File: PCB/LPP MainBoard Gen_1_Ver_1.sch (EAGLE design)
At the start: 46 parts, among them IC1 FE1.1S, J1 USB Type A, U1 MAX15070, U3 IFX007T, U4 MAX15070, U5 IFX007T, U7 Pill STM32G431, U8 Blue Pill STM32F103

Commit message: modified:   PCB/LPP MainBoard Gen_1_Ver_1.brd 	modified:   PCB/LPP MainBoard Gen_1_Ver_1.dch 	modified:   PCB/LPP MainBoard Gen_1_Ver_1.sch 	modified:   PCB/LPP_MainBoard_Gen_1_Ver_1.dip 	deleted:    PCB/LPP_MainBoard_Gen_1_Ver_1/Through.drl 	new file:   PCB/LPP_MainBoard_Gen_1_Ver_1/komtur.crv3d 	new file:   PCB/LPP_MainBoard_Gen_1_Ver_1/komtur.dxf 	new file:   PCB/LPP_MainBoard_Gen_1_Ver_1/kontur.txt
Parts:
- added R13, R14: R_0805_1206, common:R_0805_1206
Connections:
- net Сеть_10: now also R13.2
- net Сеть_6: now also R14.2
- net Сеть_7: now also R13.1, R14.1
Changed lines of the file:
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@@
 <part name="XP3" library="common" deviceset="PLS_2" device="" value="BKL  SEL"/>
 <part name="Z" library="common" deviceset="Q_1" device=""/>
+<part name="R13" library="common" deviceset="R_0805_1206" device=""/>
+<part name="R14" library="common" deviceset="R_0805_1206" device=""/>
 </parts>
 <modules/>
@@
 <text x="134.798" y="-214.63" size="1.48" layer="97" font="vector" ratio="10" rot="R0" align="bottom-left" distance="76">BKL  SEL</text>
 <text x="-81.045" y="-206.502" size="1.48" layer="97" font="vector" ratio="10" rot="R0" align="bottom-left" distance="76"></text>
+<text x="-39.135" y="-314.96" size="1.48" layer="97" font="vector" ratio="10" rot="R0" align="bottom-left" distance="76"></text>
+<text x="-39.135" y="-320.04" size="1.48" layer="97" font="vector" ratio="10" rot="R0" align="bottom-left" distance="76"></text>
 </plain>
 <moduleinsts/>
@@
 <instance part="XP3" gate="PART_1" x="140.335" y="-217.17" smashed="yes"/>
 <instance part="Z" gate="PART_1" x="-81.28" y="-208.28" smashed="yes"/>
+<instance part="R13" gate="PART_1" x="-39.37" y="-316.23" smashed="yes"/>
+<instance part="R14" gate="PART_1" x="-39.37" y="-321.31" smashed="yes"/>
 </instances>
 <busses/>
@@
 <pinref part="FPC" gate="PART_1" pin="13"/>
 <junction x="-22.86" y="-346.71"/>
-<wire layer="91" width="0.1" x1="-35.56" y1="-367.03" x2="-22.86" y2="-367.03"/>
+<wire layer="91" width="0.1" x1="-29.21" y1="-367.03" x2="-22.86" y2="-367.03"/>
+<wire layer="91" width="0.1" x1="-35.56" y1="-367.03" x2="-29.21" y2="-367.03"/>
 <pinref part="ENCKP" gate="PART_1" pin="2"/>
 <junction x="-22.86" y="-367.03"/>
+<wire layer="91" width="0.1" x1="-33.02" y1="-321.31" x2="-29.21" y2="-321.31"/>
+<wire layer="91" width="0.1" x1="-29.21" y1="-321.31" x2="-29.21" y2="-367.03"/>
+<pinref part="R14" gate="PART_1" pin="2"/>
+<junction x="-29.21" y="-367.03"/>
 </segment>
 </net>
@@
 <pinref part="NetPort12" gate="PART_1" pin="+5V"/>
 <junction x="-77.47" y="-331.47"/>
+<wire layer="91" width="0.1" x1="-46.99" y1="-321.31" x2="-46.99" y2="-331.47"/>
+<wire layer="91" width="0.1" x1="-46.99" y1="-331.47" x2="-66.04" y2="-331.47"/>
+<junction x="-46.99" y="-321.31"/>
+<wire layer="91" width="0.1" x1="-46.99" y1="-321.31" x2="-45.72" y2="-321.31"/>
+<wire layer="91" width="0.1" x1="-46.99" y1="-316.23" x2="-45.72" y2="-316.23"/>
+<wire layer="91" width="0.1" x1="-46.99" y1="-321.31" x2="-46.99" y2="-316.23"/>
+<pinref part="R14" gate="PART_1" pin="1"/>
+<pinref part="R13" gate="PART_1" pin="1"/>
+<junction x="-66.04" y="-331.47"/>
 </segment>
 <segment>
@@
 <pinref part="ENCSW" gate="PART_1" pin="2"/>
 <junction x="-24.13" y="-341.63"/>
-<wire layer="91" width="0.1" x1="-35.56" y1="-364.49" x2="-24.13" y2="-364.49"/>
+<wire layer="91" width="0.1" x1="-27.94" y1="-364.49" x2="-24.13" y2="-364.49"/>
+<wire layer="91" width="0.1" x1="-35.56" y1="-364.49" x2="-27.94" y2="-364.49"/>
 <pinref part="ENCKP" gate="PART_1" pin="3"/>
 <junction x="-24.13" y="-364.49"/>
-</segment>
-</net>
+<wire layer="91" width="0.1" x1="-33.02" y1="-316.23" x2="-27.94" y2="-316.23"/>
+<wire layer="91" width="0.1" x1="-27.94" y1="-316.23" x2="-27.94" y2="-364.49"/>
+<pinref part="R13" gate="PART_1" pin="2"/>
+<junction x="-27.94" y="-364.49"/>
+</segment>
+</net>

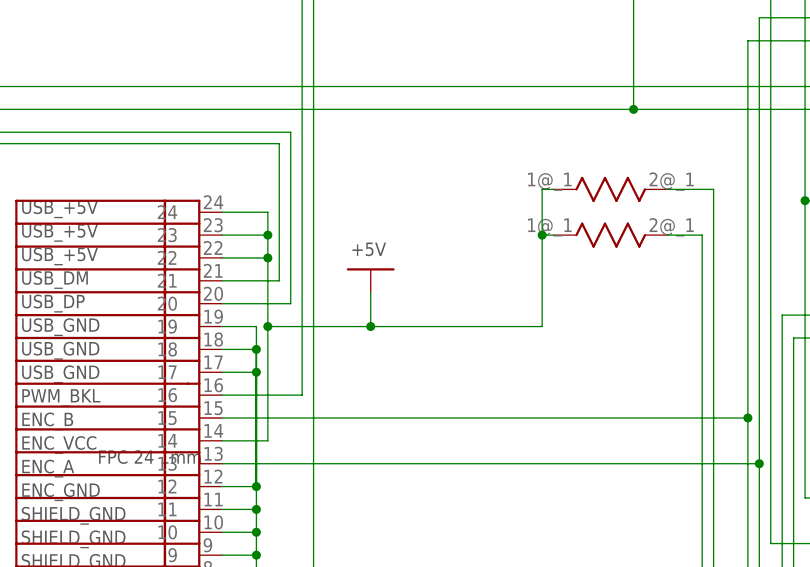
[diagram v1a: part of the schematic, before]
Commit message: modified:   PCB/LPP MainBoard Gen_1_Ver_1.brd 	modified:   PCB/LPP MainBoard Gen_1_Ver_1.dch 	modified:   PCB/LPP MainBoard Gen_1_Ver_1.sch 	modified:   PCB/LPP_MainBoard_Gen_1_Ver_1.dip 	new file:   PCB/LPP_MainBoard_Gen_1_Ver_1/Through.drl 	new file:   PCB/LPP_MainBoard_Gen_1_Ver_1/Through2.drl 	new file:   PCB/LPP_MainBoard_Gen_1_Ver_1/Through3.drl
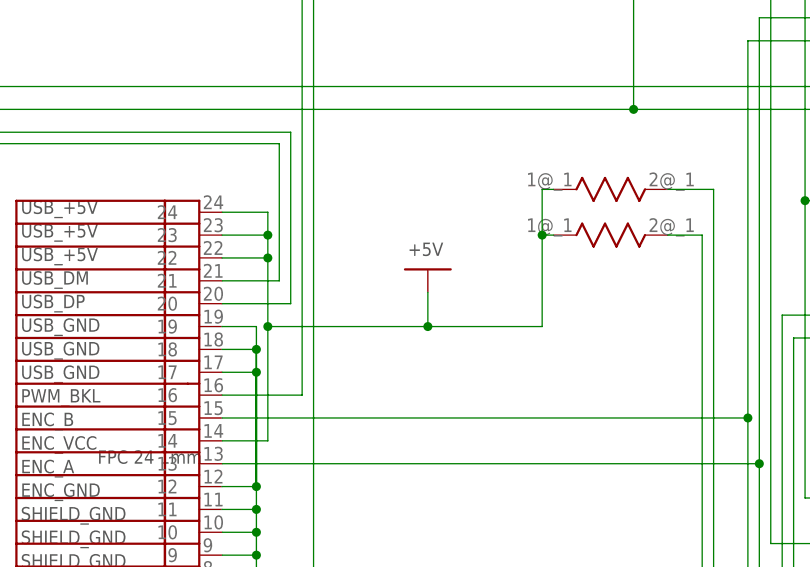
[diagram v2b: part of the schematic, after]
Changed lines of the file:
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@@
 <part name="R11" library="common" deviceset="R_0805_1206" device=""/>
 <part name="R12" library="common" deviceset="R_0805_1206" device=""/>
+<part name="R13" library="common" deviceset="R_0805_1206" device=""/>
+<part name="R14" library="common" deviceset="R_0805_1206" device=""/>
 <part name="STEPPERSHIELD" library="common" deviceset="PLS_16" device="" value="STEPPER SHIELD"/>
 <part name="U1" library="common" deviceset="MAX15070AAUT+T" device="" value="MAX15070"/>
@@
 <part name="XP3" library="common" deviceset="PLS_2" device="" value="BKL  SEL"/>
 <part name="Z" library="common" deviceset="Q_1" device=""/>
-<part name="R13" library="common" deviceset="R_0805_1206" device=""/>
-<part name="R14" library="common" deviceset="R_0805_1206" device=""/>
 </parts>
 <modules/>
@@
 <text x="-136.904" y="-374.42" size="1.48" layer="97" font="vector" ratio="10" rot="R0" align="bottom-left" distance="76">+19V</text>
 <text x="-136.525" y="-398.024" size="1.48" layer="97" font="vector" ratio="10" rot="R90" align="bottom-left" distance="76">GND</text>
-<text x="-68.26" y="-323.62" size="1.48" layer="97" font="vector" ratio="10" rot="R0" align="bottom-left" distance="76">+5V</text>
+<text x="-61.91" y="-323.62" size="1.48" layer="97" font="vector" ratio="10" rot="R0" align="bottom-left" distance="76">+5V</text>
 <text x="104.078" y="-343.94" size="1.48" layer="97" font="vector" ratio="10" rot="R0" align="bottom-left" distance="76">+19V</text>
 <text x="115.89" y="-343.94" size="1.48" layer="97" font="vector" ratio="10" rot="R0" align="bottom-left" distance="76">+5V</text>
@@
 <text x="63.735" y="-302.26" size="1.48" layer="97" font="vector" ratio="10" rot="R0" align="bottom-left" distance="76"></text>
 <text x="63.735" y="-307.34" size="1.48" layer="97" font="vector" ratio="10" rot="R0" align="bottom-left" distance="76"></text>
+<text x="-39.135" y="-314.96" size="1.48" layer="97" font="vector" ratio="10" rot="R0" align="bottom-left" distance="76"></text>
+<text x="-39.135" y="-320.04" size="1.48" layer="97" font="vector" ratio="10" rot="R0" align="bottom-left" distance="76"></text>
 <text x="95.905" y="-337.82" size="1.48" layer="97" font="vector" ratio="10" rot="R0" align="bottom-left" distance="76">STEPPER SHIELD</text>
 <text x="83.351" y="-198.12" size="1.48" layer="97" font="vector" ratio="10" rot="R0" align="bottom-left" distance="76">MAX15070</text>
@@
 <text x="134.798" y="-214.63" size="1.48" layer="97" font="vector" ratio="10" rot="R0" align="bottom-left" distance="76">BKL  SEL</text>
 <text x="-81.045" y="-206.502" size="1.48" layer="97" font="vector" ratio="10" rot="R0" align="bottom-left" distance="76"></text>
-<text x="-39.135" y="-314.96" size="1.48" layer="97" font="vector" ratio="10" rot="R0" align="bottom-left" distance="76"></text>
-<text x="-39.135" y="-320.04" size="1.48" layer="97" font="vector" ratio="10" rot="R0" align="bottom-left" distance="76"></text>
 </plain>
 <moduleinsts/>
@@
 <instance part="NetPort10" gate="PART_1" x="-134.303" y="-375.92" smashed="yes"/>
 <instance part="NetPort11" gate="PART_1" x="-134.62" y="-395.986" smashed="yes"/>
-<instance part="NetPort12" gate="PART_1" x="-66.04" y="-325.12" smashed="yes"/>
+<instance part="NetPort12" gate="PART_1" x="-59.69" y="-325.12" smashed="yes"/>
 <instance part="NetPort13" gate="PART_1" x="106.68" y="-345.44" smashed="yes"/>
 <instance part="NetPort14" gate="PART_1" x="118.11" y="-345.44" smashed="yes"/>
@@
 <instance part="R11" gate="PART_1" x="63.5" y="-303.53" smashed="yes"/>
 <instance part="R12" gate="PART_1" x="63.5" y="-308.61" smashed="yes"/>
+<instance part="R13" gate="PART_1" x="-39.37" y="-316.23" smashed="yes"/>
+<instance part="R14" gate="PART_1" x="-39.37" y="-321.31" smashed="yes"/>
 <instance part="STEPPERSHIELD" gate="PART_1" x="105.41" y="-358.14" smashed="yes"/>
 <instance part="U1" gate="PART_1" x="88.9" y="-208.28" smashed="yes"/>
@@
 <instance part="XP3" gate="PART_1" x="140.335" y="-217.17" smashed="yes"/>
 <instance part="Z" gate="PART_1" x="-81.28" y="-208.28" smashed="yes"/>
-<instance part="R13" gate="PART_1" x="-39.37" y="-316.23" smashed="yes"/>
-<instance part="R14" gate="PART_1" x="-39.37" y="-321.31" smashed="yes"/>
 </instances>
 <busses/>
@@
 <pinref part="FPC" gate="PART_1" pin="14"/>
 <junction x="-77.47" y="-323.85"/>
-<wire layer="91" width="0.1" x1="-77.47" y1="-331.47" x2="-66.04" y2="-331.47"/>
-<wire layer="91" width="0.1" x1="-66.04" y1="-331.47" x2="-66.04" y2="-327.66"/>
+<wire layer="91" width="0.1" x1="-77.47" y1="-331.47" x2="-59.69" y2="-331.47"/>
+<wire layer="91" width="0.1" x1="-59.69" y1="-331.47" x2="-59.69" y2="-327.66"/>
 <pinref part="NetPort12" gate="PART_1" pin="+5V"/>
 <junction x="-77.47" y="-331.47"/>
 <wire layer="91" width="0.1" x1="-46.99" y1="-321.31" x2="-46.99" y2="-331.47"/>
-<wire layer="91" width="0.1" x1="-46.99" y1="-331.47" x2="-66.04" y2="-331.47"/>
+<wire layer="91" width="0.1" x1="-46.99" y1="-331.47" x2="-59.69" y2="-331.47"/>
 <junction x="-46.99" y="-321.31"/>
 <wire layer="91" width="0.1" x1="-46.99" y1="-321.31" x2="-45.72" y2="-321.31"/>
@@
 <pinref part="R14" gate="PART_1" pin="1"/>
 <pinref part="R13" gate="PART_1" pin="1"/>
-<junction x="-66.04" y="-331.47"/>
-</segment>
-<segment>
+<junction x="-59.69" y="-331.47"/>
+</segment>
+<segment>

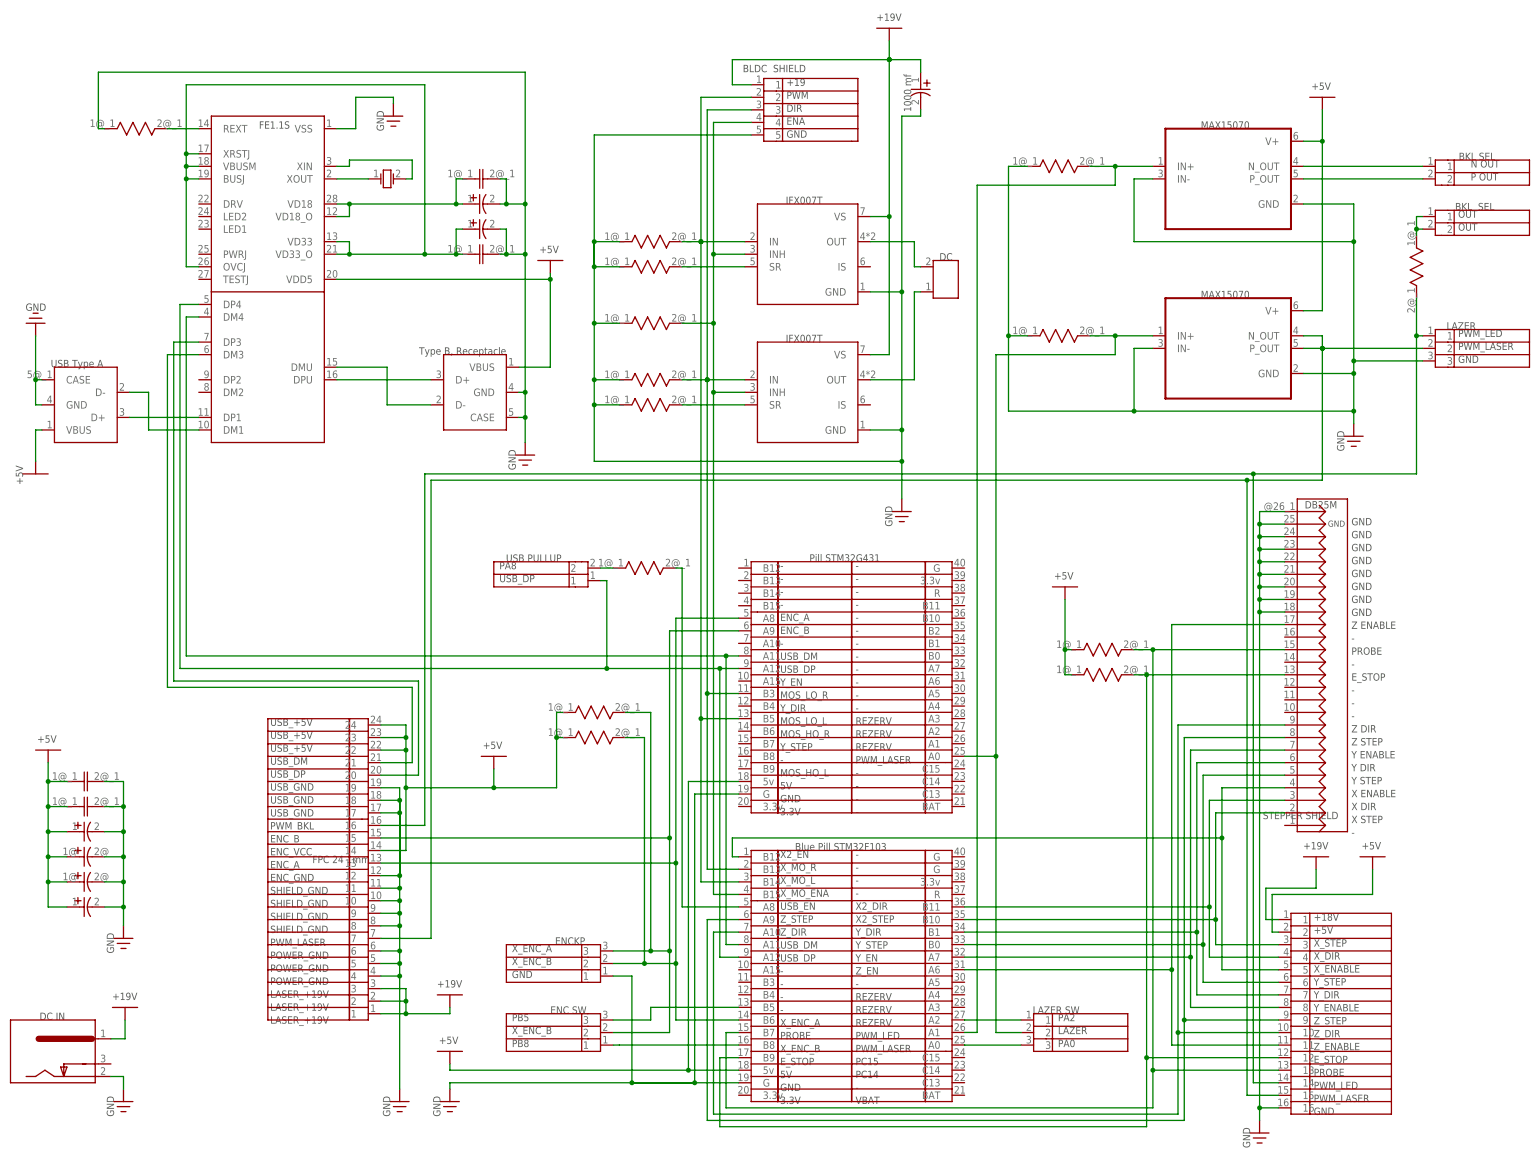
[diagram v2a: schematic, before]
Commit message: modified:   PCB/LPP MainBoard Gen_1_Ver_1.brd 	modified:   PCB/LPP MainBoard Gen_1_Ver_1.sch
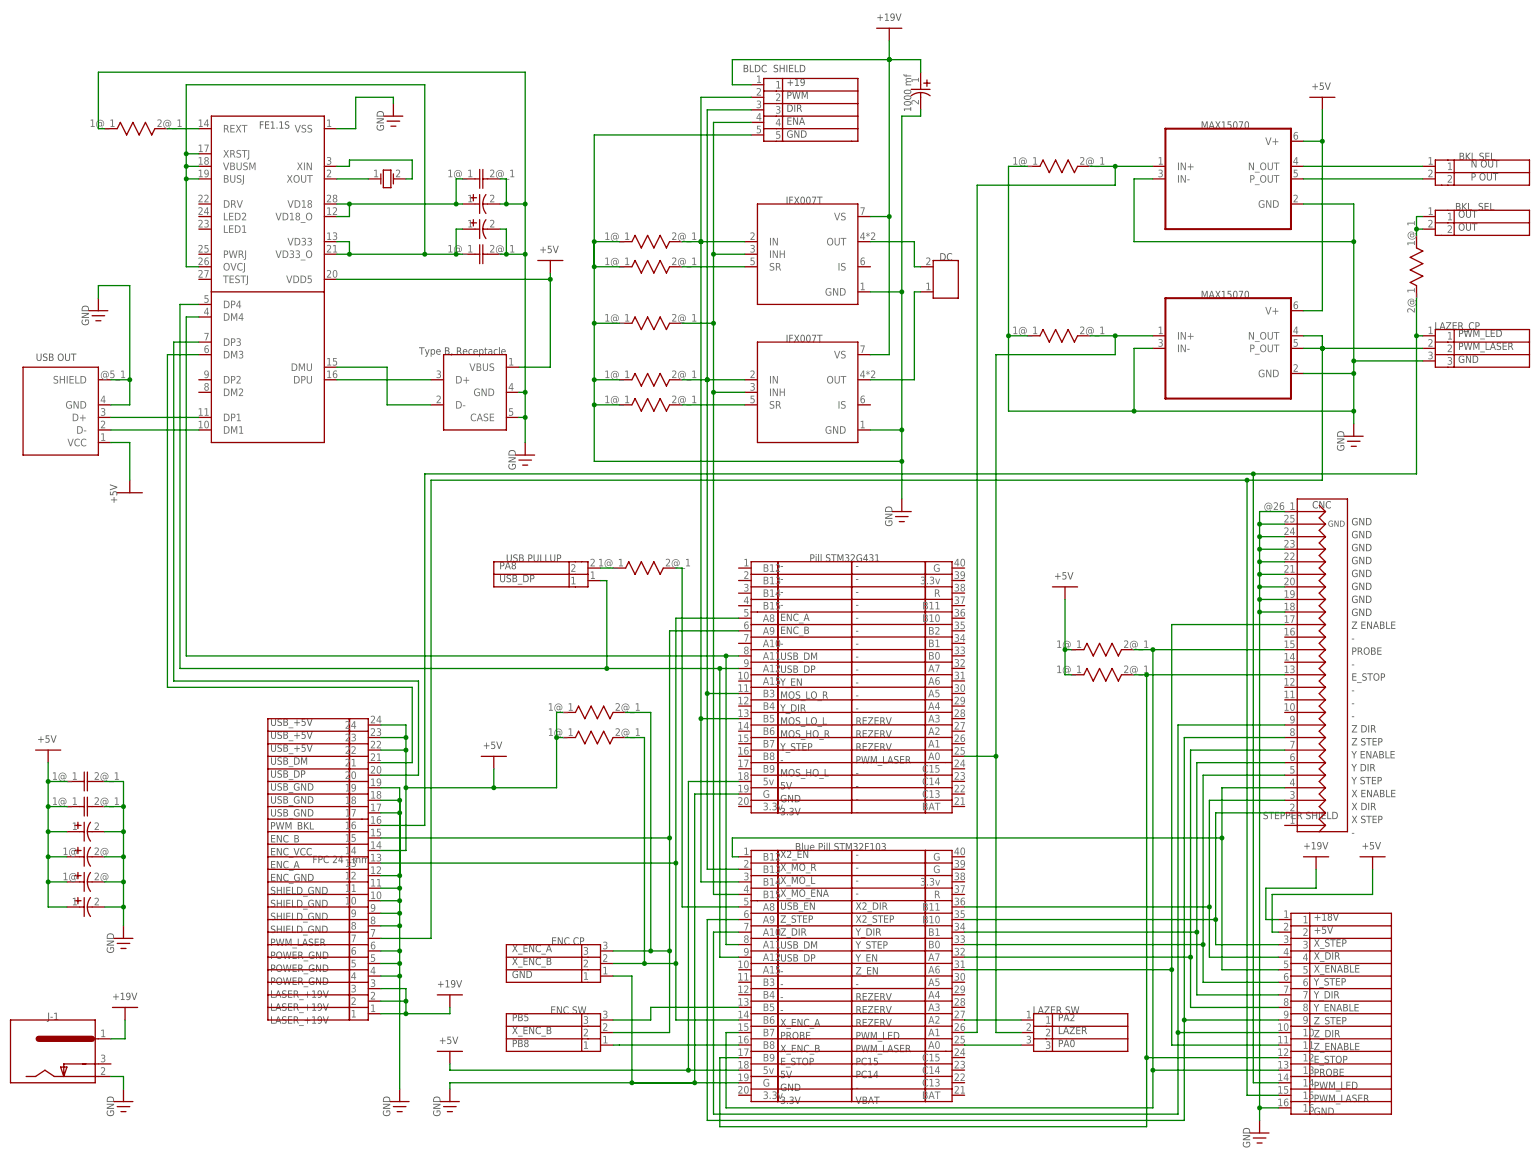
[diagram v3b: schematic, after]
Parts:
- removed J1: USB Type A, common:USB-1_TYPE_A
- added USB_OUT: USB OUT, common:USB_TYPE_A_HORIZONTAL
- CNC: value DB25M -> CNC
- DC_IN: value DC IN -> J-1
- ENC_CP: value ENCKP -> ENC CP
- LAZER_CP: value LAZER -> LAZER_CP
- renumbered DB25 to CNC, DCIN to DC_IN, ENCKP to ENC_CP, ENCSW to ENC_SW, LAZERKP to LAZER_CP, LAZERSW to LAZER_SW, STEPPERSHIELD to STEPPER_SHIELD, USBPULLUP to USB_PULLUP
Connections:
- net Сеть_0: now also USB_OUT.GND, USB_OUT.SHIELD; no longer J1.CASE, J1.GND
- net Сеть_11: now also USB_OUT.D-; no longer J1.D-
- net Сеть_7: now also USB_OUT.VCC; no longer J1.VBUS
- net Сеть_8: now also USB_OUT.D+; no longer J1.D+
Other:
- note added: "CNC"
- note added: "ENC CP"
- note added: "J-1"
- note added: "LAZER_CP"
- note added: "USB OUT"
- note removed: "DB25M"
- note removed: "DC IN"
- note removed: "ENCKP"
- note removed: "LAZER"
- note removed: "USB Type A"

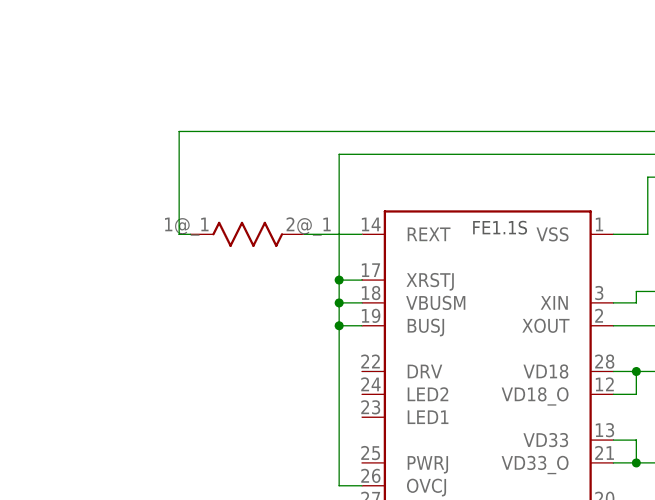
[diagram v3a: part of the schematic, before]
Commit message: modified:   PCB/LPP MainBoard Gen_1_Ver_1.sch 	modified:   PCB/LPP_MainBoard_Gen_1_Ver_1.dch 	modified:   PCB/README.md
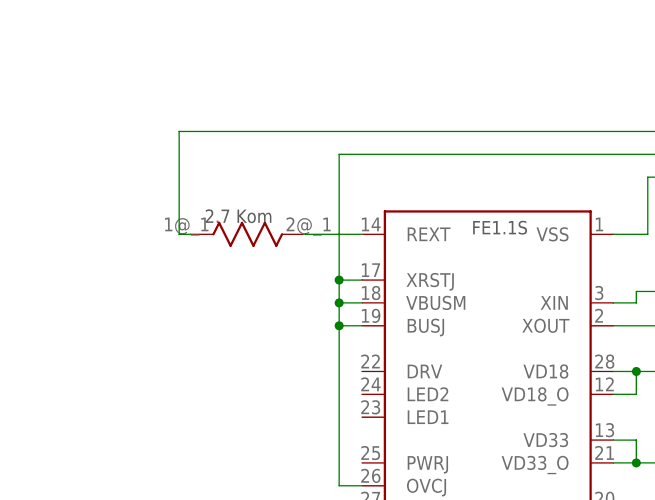
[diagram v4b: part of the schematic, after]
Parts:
- R1: value R_0805_1206 -> 2.7 Kom
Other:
- note added: "2.7 Kom"
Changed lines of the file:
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@@
 <part name="NetPort21" library="common" deviceset="+5V" device=""/>
 <part name="NetPort22" library="common" deviceset="GND" device=""/>
-<part name="R1" library="common" deviceset="R_0805_1206" device=""/>
+<part name="R1" library="common" deviceset="R_0805_1206" device="" value="2.7 Kom"/>
 <part name="R2" library="common" deviceset="R_0805_1206" device=""/>
 <part name="R3" library="common" deviceset="R_0805_1206" device=""/>
@@
 <text x="-152.08" y="-322.35" size="1.48" layer="97" font="vector" ratio="10" rot="R0" align="bottom-left" distance="76">+5V</text>
 <text x="-136.525" y="-365.004" size="1.48" layer="97" font="vector" ratio="10" rot="R90" align="bottom-left" distance="76">GND</text>
-<text x="-131.845" y="-196.85" size="1.48" layer="97" font="vector" ratio="10" rot="R0" align="bottom-left" distance="76"></text>
+<text x="-136.879" y="-196.85" size="1.48" layer="97" font="vector" ratio="10" rot="R0" align="bottom-left" distance="76">2.7 Kom</text>
 <text x="54.845" y="-204.47" size="1.48" layer="97" font="vector" ratio="10" rot="R0" align="bottom-left" distance="76"></text>
 <text x="-27.705" y="-219.71" size="1.48" layer="97" font="vector" ratio="10" rot="R0" align="bottom-left" distance="76"></text>
